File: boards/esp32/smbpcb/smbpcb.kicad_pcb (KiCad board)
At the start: 2 copper layers, 85.4 x 70.4 mm, 71 parts, among them IC1 MiCS-6814, J1 USB_B_Micro, J2 PMS7003, Q1 SUD08P06-155L, Q2 SS8050_NPN, Q3 SS8050_NPN, SW1 RESET, SW2 RESET, U1 MCP73831-2-OT, U2 SGM6603-5.0YN6G_TR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

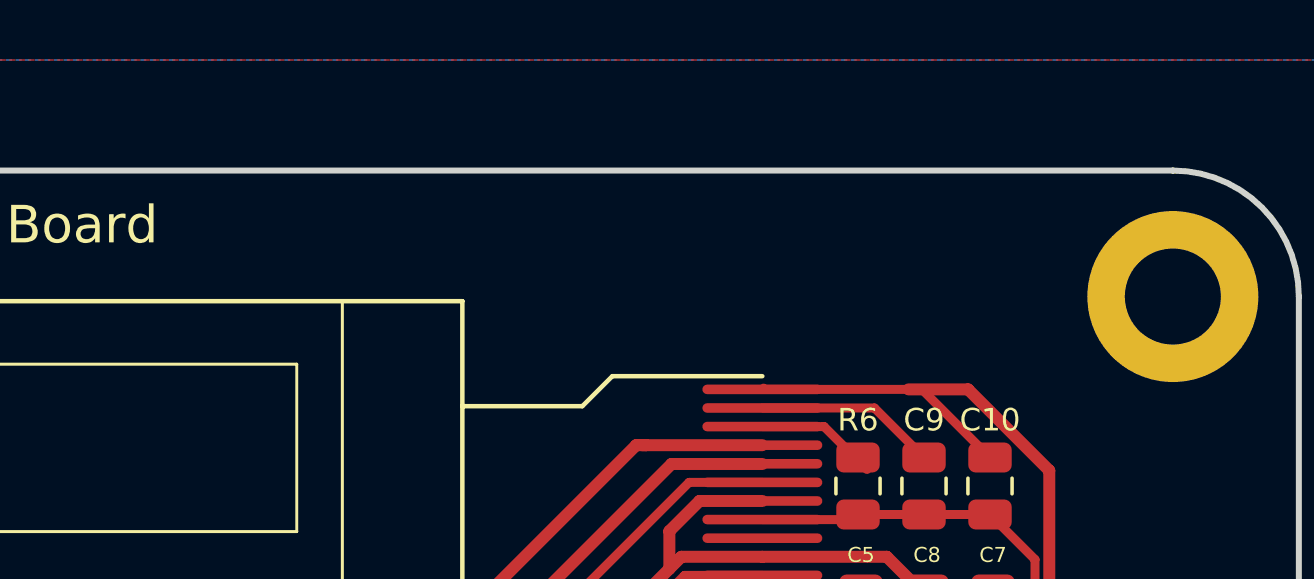
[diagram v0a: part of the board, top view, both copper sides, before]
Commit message: added silkscreen stuff
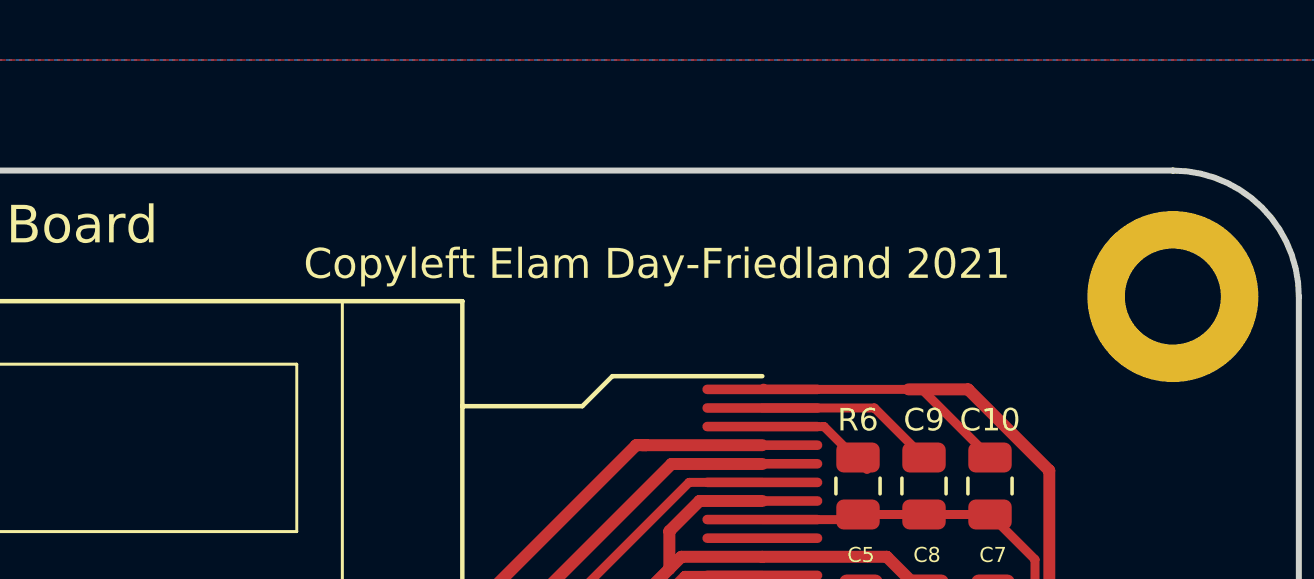
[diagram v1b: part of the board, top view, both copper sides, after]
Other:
- board text added: "Albany Loves the Air! Designed with <3 by Elam Day-Friedland with input from the AHS Air Quality Club"
- board text added: "JLCJLCJLCJLC"
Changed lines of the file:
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@@
     (fp_line (start 1.6 -0.8) (end 1.6 0.8) (layer "F.Fab") (width 0.1))
     (pad "1" smd roundrect (at -1.475 0 90) (locked) (size 1.15 1.8) (layers "F.Cu" "F.Paste" "F.Mask") (roundrect_rratio 0.2173913043478261)
-      (net 7 "+5V") (pintype "passive"))
+      (net 7 "+5V"))
     (pad "2" smd roundrect (at 1.475 0 90) (locked) (size 1.15 1.8) (layers "F.Cu" "F.Paste" "F.Mask") (roundrect_rratio 0.2173913043478261)
-      (net 1 "GND") (pintype "passive"))
+      (net 1 "GND"))
     (model "${KISYS3DMOD}/Capacitor_SMD.3dshapes/C_1206_3216Metric.wrl"
       (offset (xyz 0 0 0))
@@
   (gr_line (start 33.295 99.085) (end 110.295001 99.084999) (layer "Edge.Cuts") (width 0.2))
   (gr_line (start 29.095 32.885) (end 29.095 94.885) (layer "Edge.Cuts") (width 0.2))
-  (gr_text "Copyleft Elam Day-Friedland 2021\n" (at 65.5 97.5) (layer "B.SilkS")
-    (effects (font (size 0.75 0.75) (thickness 0.15)) (justify mirror))
+  (gr_text "Albany Loves the Air!\nDesigned with <3 by Elam Day-Friedland with input from the AHS Air Quality Club" (at 71.5 67.5) (layer "B.SilkS")
+    (effects (font (size 1.3 1.3) (thickness 0.3)) (justify mirror))
+  )
+  (gr_text "JLCJLCJLCJLC" (at 41.4 97.7) (layer "B.SilkS")
+    (effects (font (size 0.75 0.75) (thickness 0.1)) (justify mirror))
   )
   (gr_text "SDA|SCL|3V3|GND\n" (at 102.4 92.3 90) (layer "F.SilkS")
@@
     (effects (font (size 1.5 1.5) (thickness 0.3)))
   )
+  (gr_text "Copyleft Elam Day-Friedland 2021\n" (at 93.1 31.8) (layer "F.SilkS")
+    (effects (font (size 1 1) (thickness 0.15)))
+  )
   (gr_text "SDA|SCL|TX|RX\n" (at 87.5 92.5 90) (layer "F.SilkS")

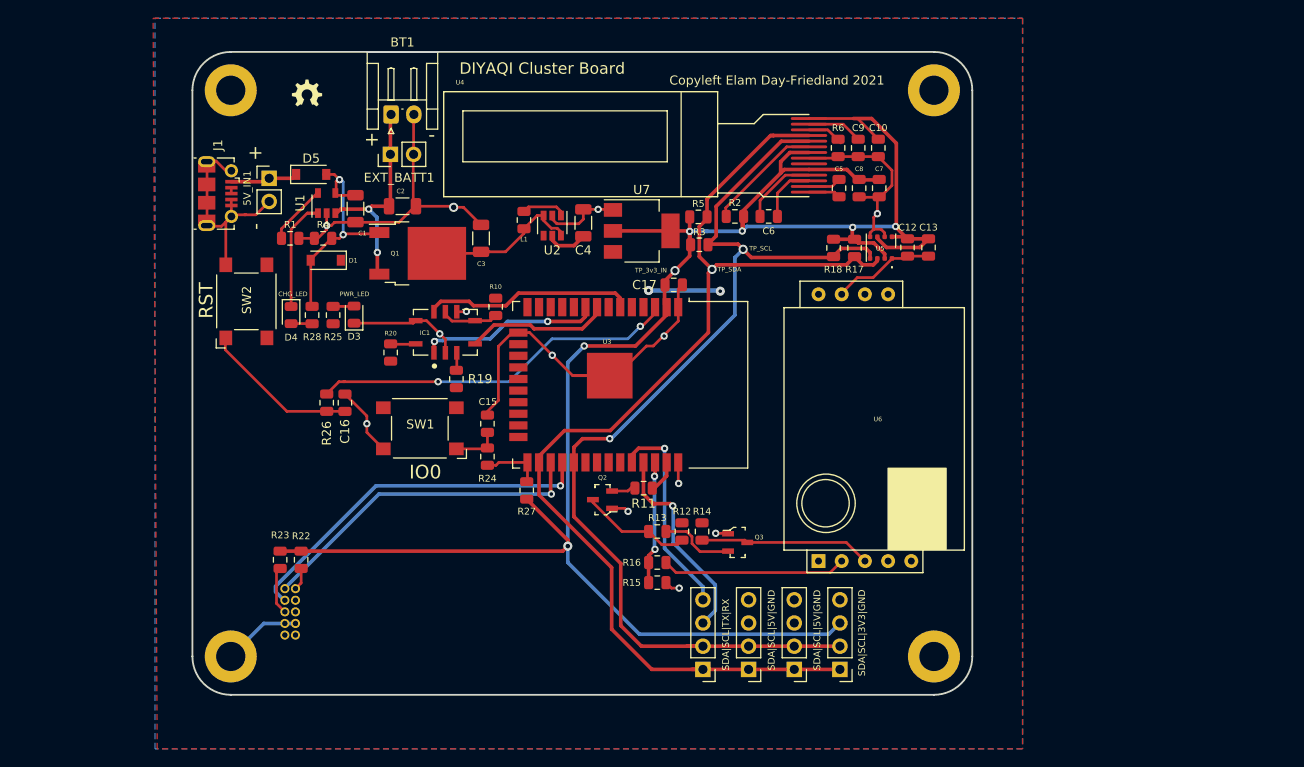
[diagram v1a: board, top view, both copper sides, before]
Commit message: switch footprints were wrong..."
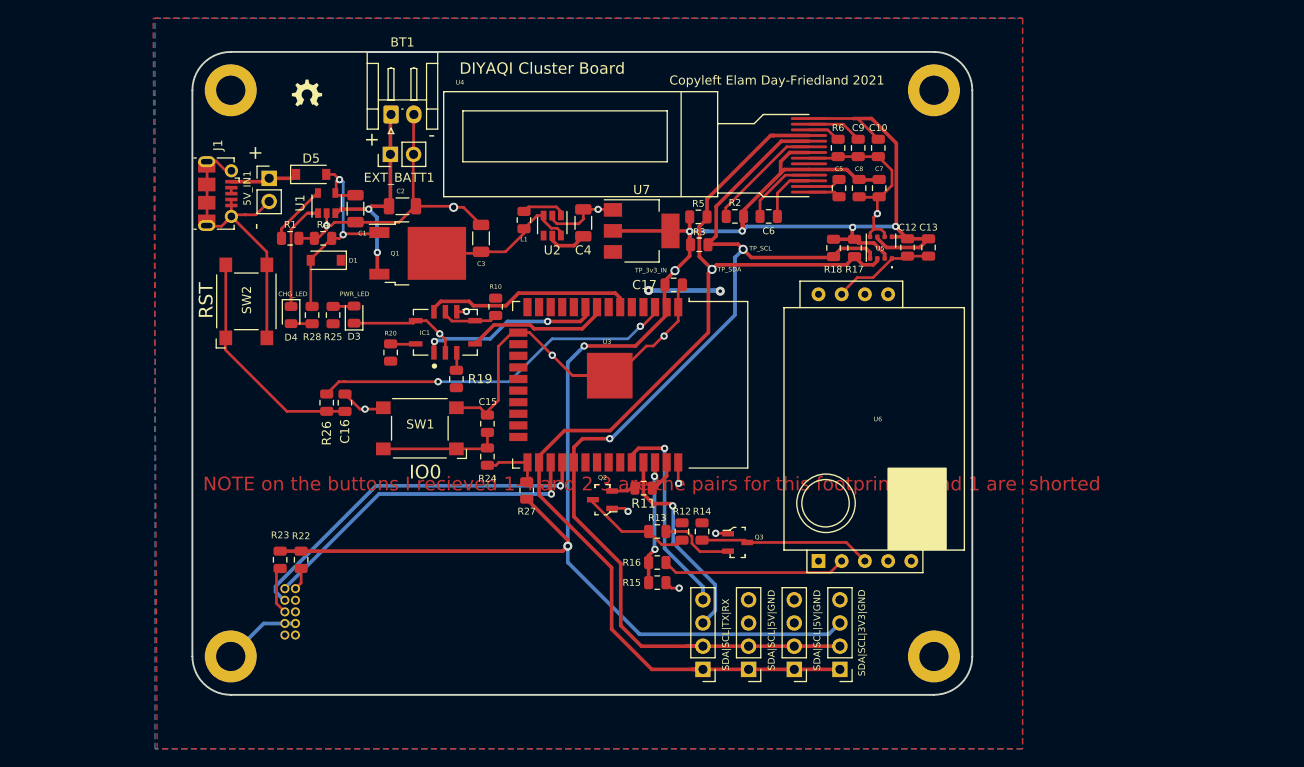
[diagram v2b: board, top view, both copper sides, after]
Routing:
- net GND: track 181.9 -> 193.1 mm
- net Net-(C15-Pad2): track 5.31 -> 13.3 mm
- net Net-(C16-Pad2): track 17.2 -> 25.2 mm
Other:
- board text added: "NOTE on the buttons I recieved 1-4 and 2-3 are the pairs for this footprint, 2 and 1 are shorted"

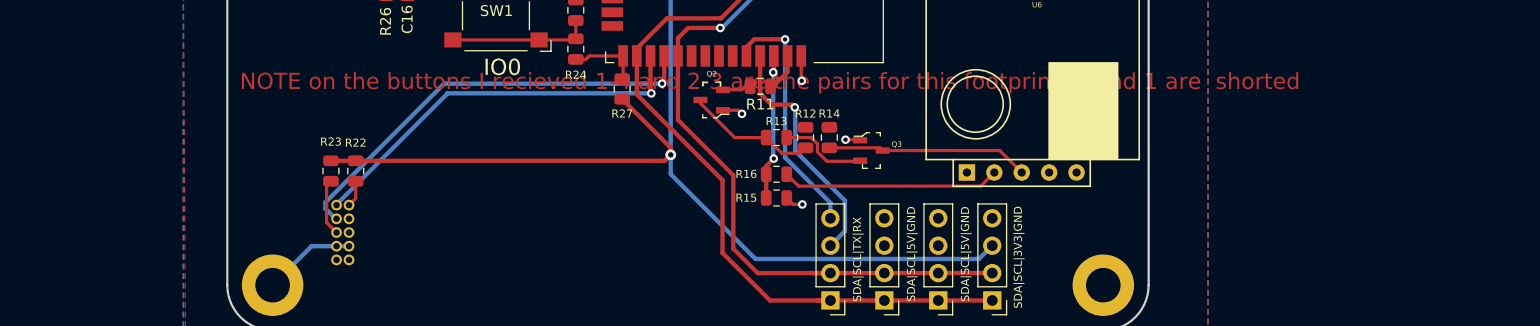
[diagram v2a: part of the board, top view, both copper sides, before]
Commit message: swapped header order to be more standard
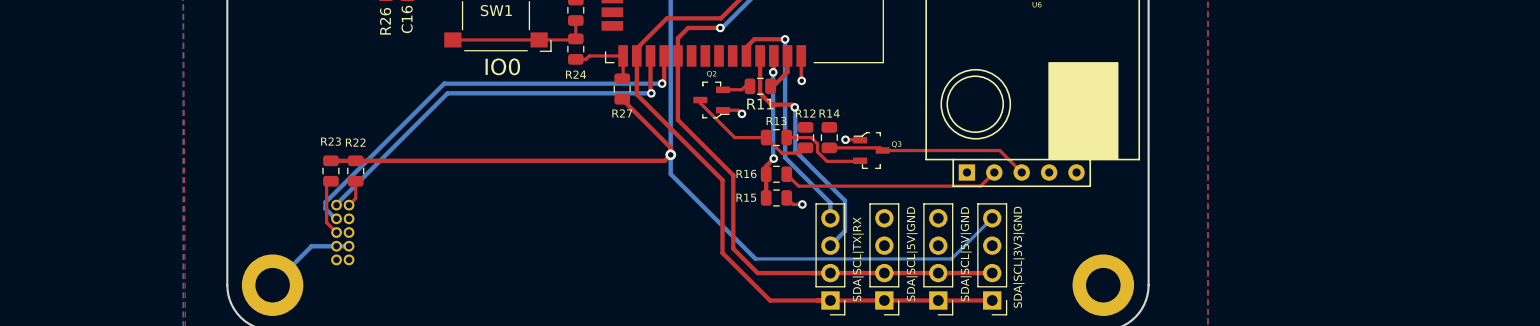
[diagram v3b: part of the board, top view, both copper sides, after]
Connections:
- AUX_CONN2 pad 3: +5V -> GND
- AUX_CONN2 pad 4: GND -> +5V
- AUX_CONN3 pad 3: +5V -> GND
- AUX_CONN3 pad 4: GND -> +5V
- AUX_CONN4 pad 3: +3V3 -> GND
- AUX_CONN4 pad 4: GND -> +3V3
- C10 pad 2: +3V3 -> Net-(C10-Pad2)
- C5 pad 1: Net-(U4-Pad1) -> Net-(C5-Pad1)
- C5 pad 2: Net-(U4-Pad2) -> Net-(C5-Pad2)
- C6 pad 1: Net-(U4-Pad4) -> Net-(C6-Pad1)
- C6 pad 2: Net-(U4-Pad3) -> Net-(C6-Pad2)
- C9 pad 2: Net-(U4-Pad13) -> Net-(C9-Pad2)
- R2 pad 2: RES -> Net-(R2-Pad2)
- R6 pad 2: Net-(U4-Pad12) -> Net-(R6-Pad2)
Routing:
- net +3V3: track 220.5 -> 221.5 mm
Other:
- board text removed: "NOTE on the buttons I recieved 1-4 and 2-3 are the pairs for this footprint, 2 and 1 are shorted"

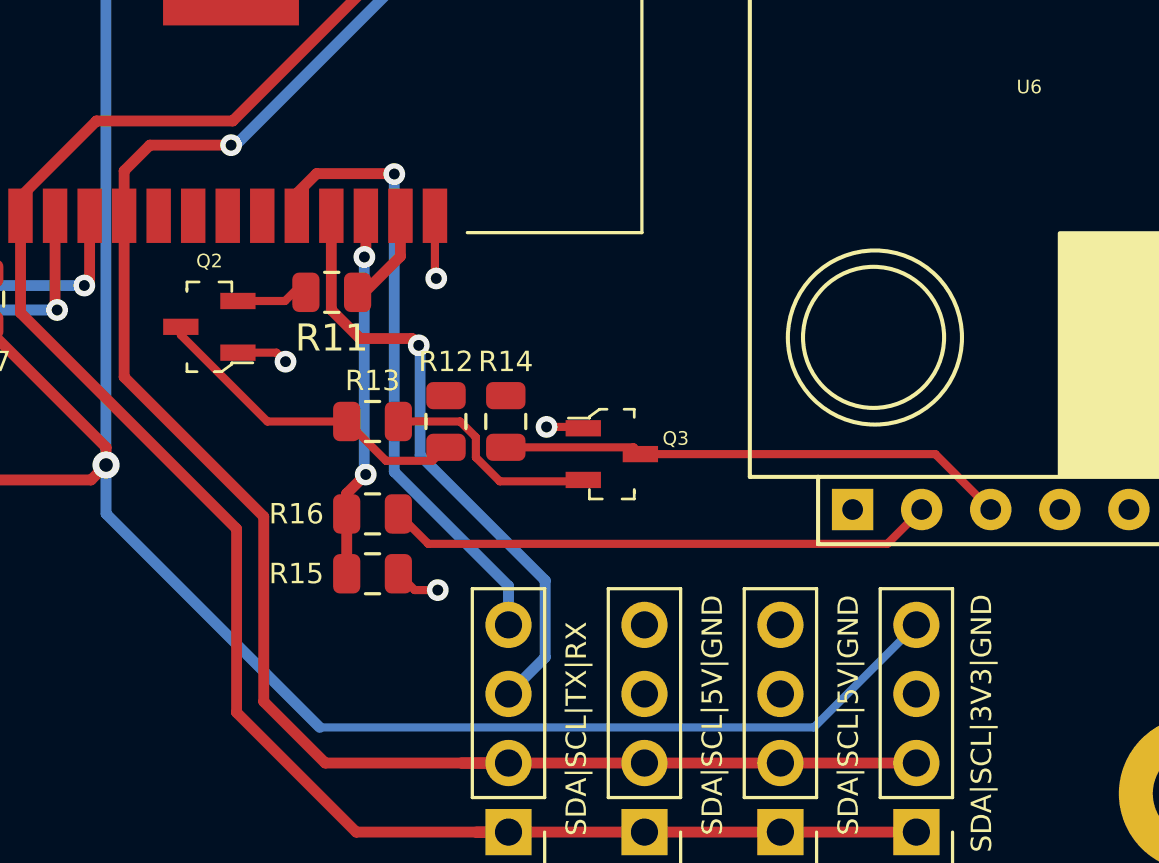
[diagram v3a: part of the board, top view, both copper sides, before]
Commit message: turns out mhz19b uses 3v3 logic and also uart doesn't work
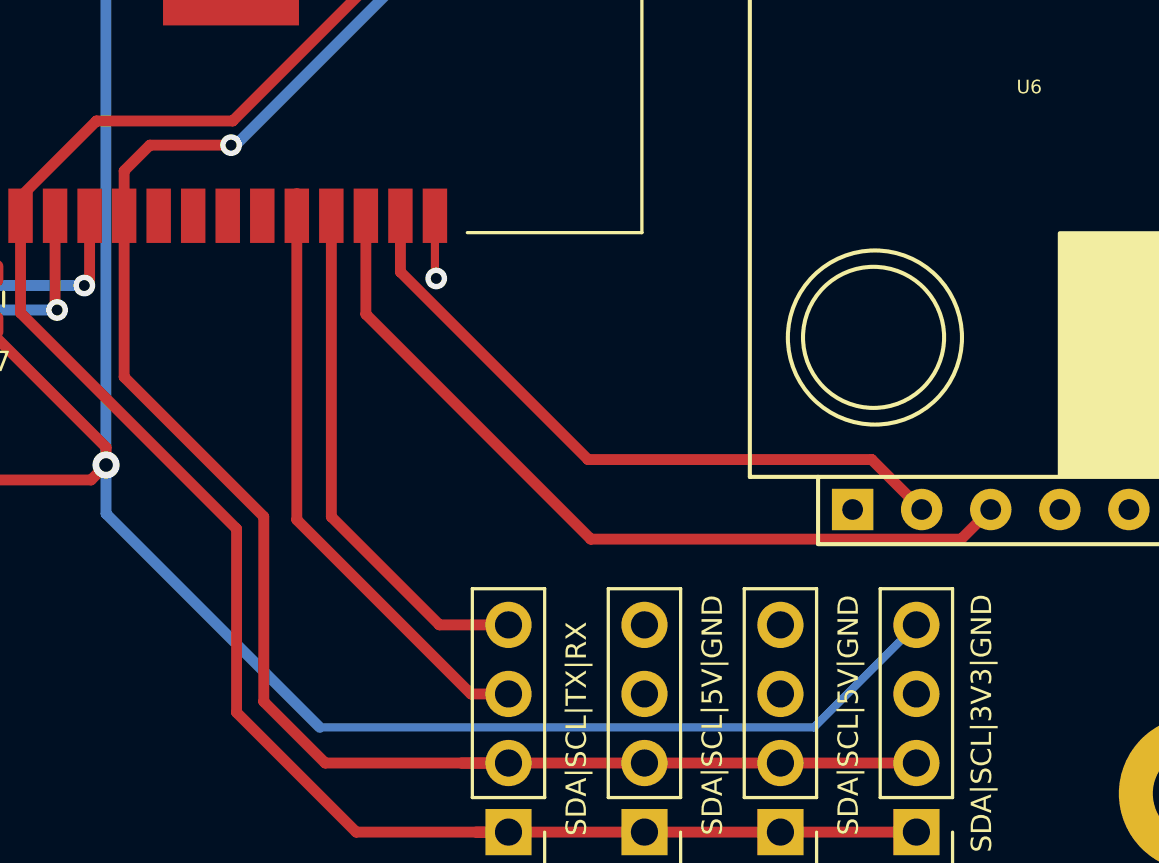
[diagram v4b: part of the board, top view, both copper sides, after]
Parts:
- removed Q2, Q3: SS8050_NPN, mics:sot-23-3
- removed R11, R12, R13, R14, R16: 1k, Capacitor_SMD:C_0805_2012Metric
- removed R15: 2k, Capacitor_SMD:C_0805_2012Metric
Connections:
- AUX_CONN1 pad 3: ESP_TX0 -> ESP_RX0
- AUX_CONN1 pad 4: ESP_RX0 -> ESP_TX0
- R27 pad 1: +3V3 -> EN
- R27 pad 2: IO0 -> +3V3
- U6 pad 2: Net-(R16-Pad2) -> ESP_RX1
- U6 pad 3: Net-(Q3-Pad3) -> ESP_TX1
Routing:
- net ESP_RX1: track 5.27 -> 26.5 mm
- net Net-(R16-Pad2): track 20.2 -> 0.00 mm
- net Net-(Q3-Pad3): track 18.8 -> 0.00 mm
- net ESP_TX1: track 13.5 -> 30.5 mm, vias 2 -> 0
- net Net-(Q2-Pad3): track 12.2 -> 0.00 mm
- net Net-(Q3-Pad2): track 7.58 -> 0.00 mm
- net GND: track 193.1 -> 188.5 mm, vias 13 -> 10
- net ESP_TX0: track 23.0 -> 19.2 mm, vias 1 -> 0
- net Net-(Q2-Pad2): track 2.39 -> 0.00 mm
- net ESP_RX0: track 23.0 -> 22.7 mm, vias 1 -> 0

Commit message: mics sucks lol
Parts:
- added R7: 220k, Capacitor_SMD:C_0805_2012Metric, F.Cu at (65.4, 53.6)
- added R8: 220k, Capacitor_SMD:C_0805_2012Metric, F.Cu at (60.8, 63.7)
- added R9: 68k, Capacitor_SMD:C_0805_2012Metric, F.Cu at (53.3, 63.7)
- moved R27 26.2 mm to (78.0, 53.6)
- moved AUX_CONN1 18.0 mm to (82.7, 78.4), turned to 0 degrees
- moved D3 2.50 mm to (44.3, 57.4)
- moved R25 1.90 mm to (46.4, 57.4), turned to -90 degrees
- moved SW1 0.45 mm to (53.8, 70.3)
- turned R22 to -90 degrees
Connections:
- AUX_CONN1 pad 1: SDA -> ESP_TX1
- AUX_CONN1 pad 2: SCL -> ESP_RX1
- AUX_CONN1 pad 3: ESP_RX0 -> ESP_TX0
- AUX_CONN1 pad 4: ESP_TX0 -> ESP_RX0
- R22 pad 1: Net-(J2-Pad10) -> +3V3
- R22 pad 2: +3V3 -> Net-(J2-Pad10)
- U3 pad 33: unconnected-(U3-Pad33) -> pwm_mhz19b
- U3 pad 36: ESP_TX1 -> ESP_RX1
- U3 pad 37: ESP_RX1 -> ESP_TX1
- U6 pad 2: ESP_RX1 -> unconnected-(U6-Pad2)
- U6 pad 3: ESP_TX1 -> unconnected-(U6-Pad3)
- U6 pad 9: unconnected-(U6-Pad9) -> pwm_mhz19b
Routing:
- net pwm_mhz19b: track 0.00 -> 37.4 mm
- net ESP_TX1: track 30.5 -> 7.12 mm
- net ESP_RX1: track 26.5 -> 8.52 mm
- net ESP_TX0: track 19.2 -> 11.6 mm
- net ESP_RX0: track 22.7 -> 15.5 mm
- net +3V3: track 221.5 -> 215.3 mm, vias 7 -> 6
- net +5V: track 13.1 -> 18.5 mm
- net EN: track 40.5 -> 44.5 mm
- net NO2: track 20.0 -> 22.6 mm
- net NH3: track 15.8 -> 18.2 mm
- net IO0: track 6.67 -> 4.52 mm
- net GND: track 188.5 -> 189.8 mm
- net Net-(D3-Pad2): track 2.33 -> 3.11 mm
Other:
- board text added: "RX0|TX0|RX1|TX1"
- board text added: "SDA|SCL|GND|3V3"
- board text added: "SDA|SCL|GND|5V"
- board text removed: "SDA|SCL|3V3|GND"
- board text removed: "SDA|SCL|5V|GND"
- board text removed: "SDA|SCL|TX|RX"
